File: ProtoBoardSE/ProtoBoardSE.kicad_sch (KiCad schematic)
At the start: 32 parts, among them J1 TYPE-C-31-M-12, J10 Conn_01x05, J11 Conn_01x05_Female, J2 TYPE-C-31-M-12, J3 Conn_01x10_Female, J4 Conn_01x05_Female, J5 Conn_01x05, J6 Conn_01x05, J7 Conn_01x05_Female, J8 Conn_01x05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

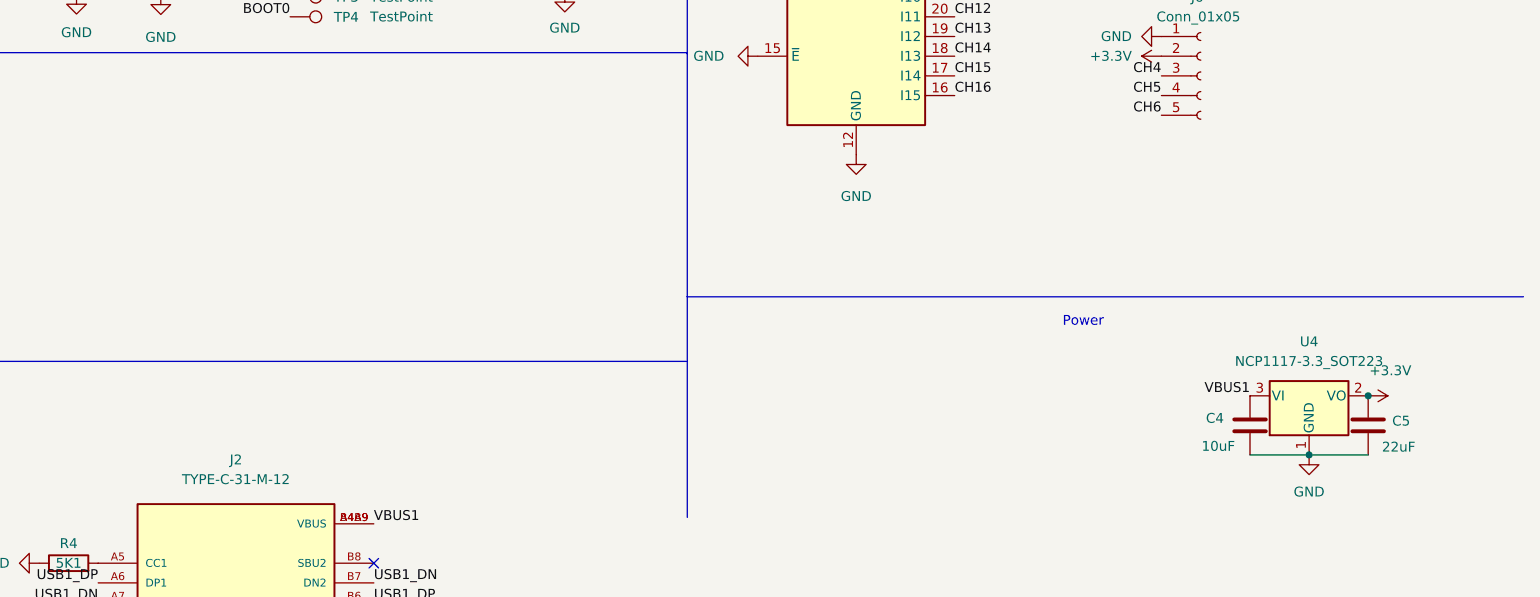
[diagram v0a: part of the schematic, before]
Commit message: ProtoBoard SE : fix capacitor value and add reset/boot button
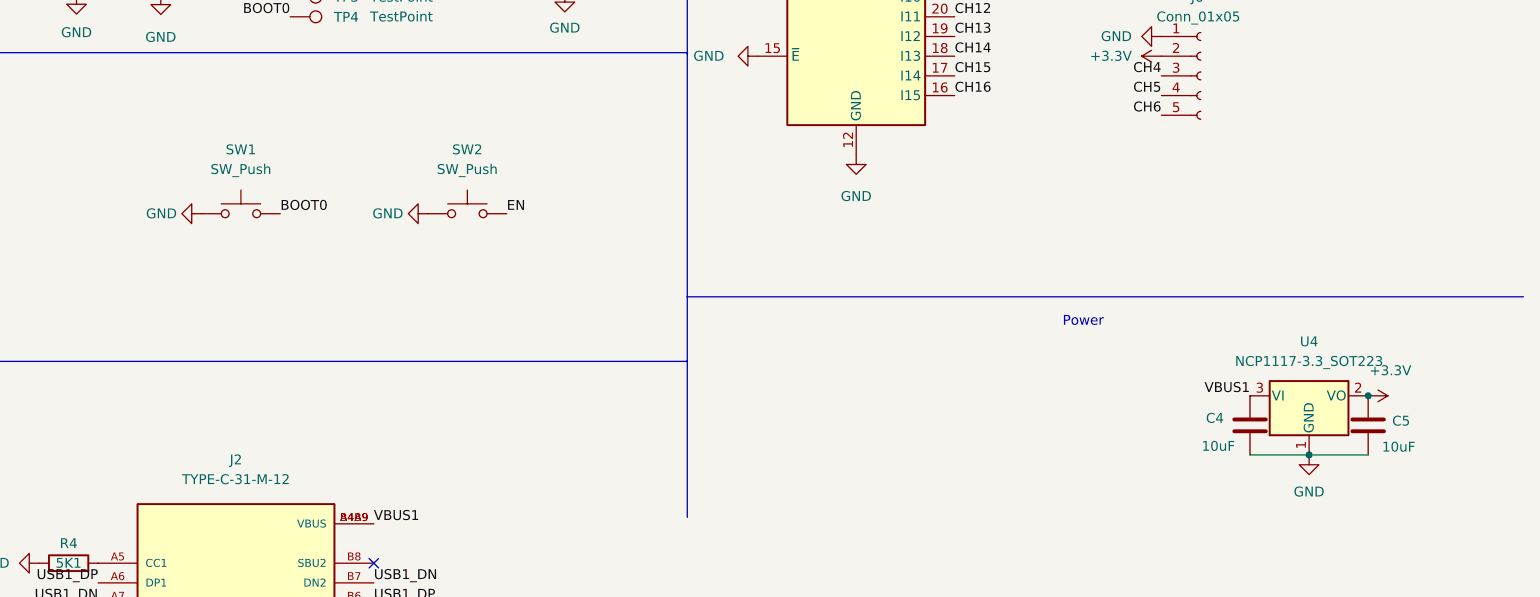
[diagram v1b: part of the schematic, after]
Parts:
- added SW1, SW2: SW_Push, Button_Switch_SMD:SW_Push_1P1T_NO_CK_KMR2, symbol Switch:SW_Push
- C5: value 22uF -> 10uF
- J1, J2: LCSC (none) -> C165948
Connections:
- net BOOT0: now also SW1.2
- net EN: now also SW2.2
- net GND: now also SW1.1, SW2.1
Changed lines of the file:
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@@
     (effects (font (size 1.27 1.27)) (justify right bottom))
+  )
+  (label "EN" (at 156.845 127.635 0)
+    (effects (font (size 1.27 1.27)) (justify left bottom))
   )
   (label "USB0_DP" (at 30.48 174.625 180)
@@
   (label "SEL1" (at 189.23 89.535 180)
     (effects (font (size 1.27 1.27)) (justify right bottom))
+  )
+  (label "BOOT0" (at 127.635 127.635 0)
+    (effects (font (size 1.27 1.27)) (justify left bottom))
   )
   (label "CH5" (at 241.3 112.395 180)
@@
     (property "STANDARD" "Manufacturer Recommendations" (id 7) (at 48.26 177.165 0)
       (effects (font (size 1.27 1.27)) (justify left bottom) hide)
+    )
+    (property "LCSC" "C165948" (id 8) (at 48.26 177.165 0)
+      (effects (font (size 1.27 1.27)) hide)
     )
     (pin "A1B12")
@@
       (effects (font (size 1.27 1.27)) (justify left bottom) hide)
     )
+    (property "LCSC" "C165948" (id 8) (at 121.92 177.8 0)
+      (effects (font (size 1.27 1.27)) hide)
+    )
     (pin "A1B12")
     (pin "A4B9")
@@
   )
   (symbol (lib_id "Device:C") (at 168.91 95.25 0) (unit 1)
-    (in_bom yes) (on_board yes) (fields_autoplaced)
+    (in_bom yes) (on_board yes)
     (property "Reference" "C3" (id 0) (at 172.9232 93.9799 0)
       (effects (font (size 1.27 1.27)) (justify left))
@@
     )
     (pin "1")
+  )
+  (symbol (lib_id "Switch:SW_Push") (at 151.765 127.635 0) (unit 1)
+    (in_bom yes) (on_board yes) (fields_autoplaced)
+    (property "Reference" "SW2" (id 0) (at 151.765 119.38 0))
+    (property "Value" "SW_Push" (id 1) (at 151.765 121.92 0))
+    (property "Footprint" "Button_Switch_SMD:SW_Push_1P1T_NO_CK_KMR2" (id 2) (at 151.765 122.555 0)
+      (effects (font (size 1.27 1.27)) hide)
+    )
+    (property "Datasheet" "~" (id 3) (at 151.765 122.555 0)
+      (effects (font (size 1.27 1.27)) hide)
+    )
+    (pin "1")
+    (pin "2")
   )
   (symbol (lib_id "power:GND") (at 66.04 186.055 90) (unit 1)
@@
       (effects (font (size 1.27 1.27)) (justify left))
     )
-    (property "Value" "22uF" (id 1) (at 269.748 157.734 0)
+    (property "Value" "10uF" (id 1) (at 269.748 157.734 0)
       (effects (font (size 1.27 1.27)) (justify left))
     )
@@
     )
     (pin "1")
+  )
+  (symbol (lib_id "Switch:SW_Push") (at 122.555 127.635 0) (unit 1)
+    (in_bom yes) (on_board yes) (fields_autoplaced)
+    (property "Reference" "SW1" (id 0) (at 122.555 119.38 0))
+    (property "Value" "SW_Push" (id 1) (at 122.555 121.92 0))
+    (property "Footprint" "Button_Switch_SMD:SW_Push_1P1T_NO_CK_KMR2" (id 2) (at 122.555 122.555 0)
+      (effects (font (size 1.27 1.27)) hide)
+    )
+    (property "Datasheet" "~" (id 3) (at 122.555 122.555 0)
+      (effects (font (size 1.27 1.27)) hide)
+    )
+    (pin "1")
+    (pin "2")
   )
   (symbol (lib_id "Device:R") (at 143.51 180.34 90) (unit 1)
@@
     (pin "2")
   )
+  (symbol (lib_id "power:GND") (at 146.685 127.635 270) (unit 1)
+    (in_bom yes) (on_board yes) (fields_autoplaced)
+    (property "Reference" "#PWR0118" (id 0) (at 140.335 127.635 0)
+      (effects (font (size 1.27 1.27)) hide)
+    )
+    (property "Value" "GND" (id 1) (at 143.51 127.6349 90)
+      (effects (font (size 1.27 1.27)) (justify right))
+    )
+    (property "Footprint" "" (id 2) (at 146.685 127.635 0)
+      (effects (font (size 1.27 1.27)) hide)
+    )
+    (property "Datasheet" "" (id 3) (at 146.685 127.635 0)
+      (effects (font (size 1.27 1.27)) hide)
+    )
+    (pin "1")
+  )
   (symbol (lib_id "power:GND") (at 156.21 83.82 90) (unit 1)
     (in_bom yes) (on_board yes) (fields_autoplaced)
@@
     (pin "5")
   )
+  (symbol (lib_id "power:GND") (at 117.475 127.635 270) (unit 1)
+    (in_bom yes) (on_board yes) (fields_autoplaced)
+    (property "Reference" "#PWR0117" (id 0) (at 111.125 127.635 0)
+      (effects (font (size 1.27 1.27)) hide)
+    )
+    (property "Value" "GND" (id 1) (at 114.3 127.6349 90)
+      (effects (font (size 1.27 1.27)) (justify right))
+    )
+    (property "Footprint" "" (id 2) (at 117.475 127.635 0)
+      (effects (font (size 1.27 1.27)) hide)
+    )
+    (property "Datasheet" "" (id 3) (at 117.475 127.635 0)
+      (effects (font (size 1.27 1.27)) hide)
+    )
+    (pin "1")
+  )
   (symbol (lib_id "power:GND") (at 96.52 172.72 270) (unit 1)
     (in_bom yes) (on_board yes) (fields_autoplaced)
@@
       (reference "#PWR0116") (unit 1) (value "+3.3V") (footprint "")
     )
+    (path "/f5d81395-1851-47d7-9b16-86c461d502b9"
+      (reference "#PWR0117") (unit 1) (value "GND") (footprint "")
+    )
+    (path "/c8779e0b-0142-4057-9eba-d8f816a71226"
+      (reference "#PWR0118") (unit 1) (value "GND") (footprint "")
+    )
     (path "/48ffa39d-adda-4d9d-99bf-b54fa3fc4beb"
       (reference "#PWR0119") (unit 1) (value "GND") (footprint "")
@@
     )
     (path "/6916b03b-1110-449f-9f3c-ab347cf003e7"
-      (reference "C5") (unit 1) (value "22uF") (footprint "Capacitor_SMD:C_0402_1005Metric")
+      (reference "C5") (unit 1) (value "10uF") (footprint "Capacitor_SMD:C_0402_1005Metric")
     )
     (path "/47102c41-05df-4da0-a689-4e4c5e60d6aa"
@@
       (reference "R5") (unit 1) (value "5K1") (footprint "Resistor_SMD:R_0402_1005Metric")
     )
+    (path "/bcfb42cf-0e45-48dc-8205-cd15ae8959ae"
+      (reference "SW1") (unit 1) (value "SW_Push") (footprint "Button_Switch_SMD:SW_Push_1P1T_NO_CK_KMR2")
+    )
+    (path "/539bcfcd-95f9-4be8-b514-7875fd29ac14"
+      (reference "SW2") (unit 1) (value "SW_Push") (footprint "Button_Switch_SMD:SW_Push_1P1T_NO_CK_KMR2")
+    )
     (path "/43606ef2-14fd-4069-ae54-3abba668fc58"

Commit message: ProtoBoard SE : part sourcing
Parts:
- removed U1: ESP32-S3-WROOM-2, Espressif:ESP32-S3-WROOM-2, symbol Espressif:ESP32-S3-WROOM-2
- added C6: 0.1uF, Capacitor_SMD:C_0402_1005Metric, symbol Device:C
- added U1: ESP32-S3-WROOM-1, Espressif:ESP32-S3-WROOM-1, symbol Espressif:ESP32-S3-WROOM-1
- C1, C3: LCSC (none) -> C129131
- C2: LCSC (none) -> C415703
- C4, C5: LCSC (none) -> C315248
- J10, J5, J6, J8, J9: footprint Connector_JST:JST_XA_B05B-XASK-1-A_1x05_P2.50mm_Vertical -> Connector_JST:JST_XH_B5B-XH-AM_1x05_P2.50mm_Vertical; LCSC (none) -> C161872
- J11, J4, J7: LCSC (none) -> C492404
- J3: LCSC (none) -> C495726
- R1, R3, R4, R5: LCSC (none) -> C105872
- R2: LCSC (none) -> C427247
- SW1, SW2: LCSC (none) -> C221678
- U2: LCSC (none) -> C496123
- U4: LCSC (none) -> C146799
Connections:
- net +3V3: now also C6.1, U1.2 (3V3)
- net BOOT0: now also U1.27 (GPIO0/BOOT)
- net ButA: now also U1.12 (GPIO8/TOUCH8/ADC1_CH7/SUBSPICS1)
- net ButB: now also U1.6 (GPIO6/TOUCH6/ADC1_CH5)
- net ButC: now also U1.5 (GPIO5/TOUCH5/ADC1_CH4)
- net ButJ: now also U1.4 (GPIO4/TOUCH4/ADC1_CH3)
- net COM1: now also U1.39 (GPIO1/TOUCH1/ADC1_CH0)
- net EN: now also U1.3 (EN)
- net GND: now also C6.2, U1.1 (GND), U1.40 (GND), U1.41 (GND)
- net JoyX: now also U1.38 (GPIO2/TOUCH2/ADC1_CH1)
- net JoyY: now also U1.15 (GPIO3/TOUCH3/ADC1_CH2)
- net Menu: now also U1.7 (GPIO7/TOUCH7/ADC1_CH6)
- net RXD0: now also U1.36 (U0RXD/GPIO44/CLK_OUT2)
- net SEL1: now also U1.26 (GPIO45)
- net SEL2: now also U1.25 (GPIO48/SPICLK_N/SUBSPICLK_N_DIFF)
- net SEL3: now also U1.24 (GPIO47/SPICLK_P/SUBSPICLK_P_DIFF)
- net SEL4: now also U1.23 (GPIO21)
- net Servo1: now also U1.35 (MTMS/GPIO42)
- net Servo2: now also U1.34 (MTDI/GPIO41/CLK_OUT1)
- net Servo3: now also U1.33 (MTDO/GPIO40/CLK_OUT2)
- net Servo4: now also U1.32 (MTCK/GPIO39/CLK_OUT3/SUBSPICS1)
- net Servo5: now also U1.31 (GPIO38/FSPIWP/SUBSPIWP)
- net TXD0: now also U1.37 (U0TXD/GPIO43/CLK_OUT1)
- net USB1_DN: now also U1.13 (GPIO19/U1RTS/ADC2_CH8/CLK_OUT2/USB_D-)
- net USB1_DP: now also U1.14 (GPIO20/U1CTS/ADC2_CH9/CLK_OUT1/USB_D+)
- no-connect marks 13 -> 19

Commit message: ProtoBoard SE : production files for JLCPCB
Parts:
- H1, H2, H3, H4: footprint MountingHole:MountingHole_2.2mm_M2_Pad -> MountingHole:MountingHole_2.2mm_M2
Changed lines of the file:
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@@
       (effects (font (size 1.27 1.27)) (justify left))
     )
-    (property "Footprint" "MountingHole:MountingHole_2.2mm_M2_Pad" (id 2) (at 101.346 96.7994 0)
+    (property "Footprint" "MountingHole:MountingHole_2.2mm_M2" (id 2) (at 101.346 96.7994 0)
       (effects (font (size 1.27 1.27)) hide)
     )
@@
       (effects (font (size 1.27 1.27)) (justify left))
     )
-    (property "Footprint" "MountingHole:MountingHole_2.2mm_M2_Pad" (id 2) (at 73.66 97.0026 0)
+    (property "Footprint" "MountingHole:MountingHole_2.2mm_M2" (id 2) (at 73.66 97.0026 0)
       (effects (font (size 1.27 1.27)) hide)
     )
@@
       (effects (font (size 1.27 1.27)) (justify left))
     )
-    (property "Footprint" "MountingHole:MountingHole_2.2mm_M2_Pad" (id 2) (at 112.2172 96.8502 0)
+    (property "Footprint" "MountingHole:MountingHole_2.2mm_M2" (id 2) (at 112.2172 96.8502 0)
       (effects (font (size 1.27 1.27)) hide)
     )
@@
       (effects (font (size 1.27 1.27)) (justify left))
     )
-    (property "Footprint" "MountingHole:MountingHole_2.2mm_M2_Pad" (id 2) (at 88.6968 96.7994 0)
+    (property "Footprint" "MountingHole:MountingHole_2.2mm_M2" (id 2) (at 88.6968 96.7994 0)
       (effects (font (size 1.27 1.27)) hide)
     )
@@
     )
     (path "/47102c41-05df-4da0-a689-4e4c5e60d6aa"
-      (reference "H1") (unit 1) (value "MH") (footprint "MountingHole:MountingHole_2.2mm_M2_Pad")
+      (reference "H1") (unit 1) (value "MH") (footprint "MountingHole:MountingHole_2.2mm_M2")
     )
     (path "/de51e245-a27c-4a43-a9d6-150e7ff82e45"
-      (reference "H2") (unit 1) (value "MH") (footprint "MountingHole:MountingHole_2.2mm_M2_Pad")
+      (reference "H2") (unit 1) (value "MH") (footprint "MountingHole:MountingHole_2.2mm_M2")
     )
     (path "/2a126e98-5b44-4ec5-af47-80fdf2a7b11b"
-      (reference "H3") (unit 1) (value "MH") (footprint "MountingHole:MountingHole_2.2mm_M2_Pad")
+      (reference "H3") (unit 1) (value "MH") (footprint "MountingHole:MountingHole_2.2mm_M2")
     )
     (path "/4dc08b0e-cf74-4295-b811-c24343b38bbd"
-      (reference "H4") (unit 1) (value "MH") (footprint "MountingHole:MountingHole_2.2mm_M2_Pad")
+      (reference "H4") (unit 1) (value "MH") (footprint "MountingHole:MountingHole_2.2mm_M2")
     )
     (path "/37122a64-2a17-4ee6-b1f9-f5f5d25e945b"
